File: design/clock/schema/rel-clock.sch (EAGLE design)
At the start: 15 parts, among them Q1 BC556, Q2 BS170

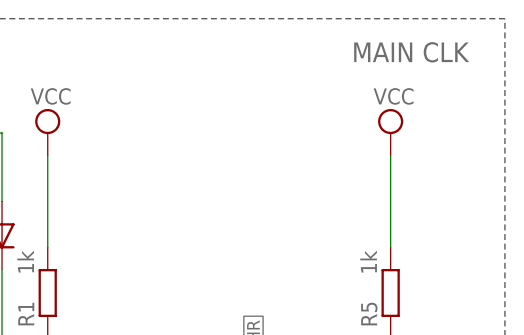
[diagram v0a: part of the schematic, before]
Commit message: Aligned titles size for all schemas
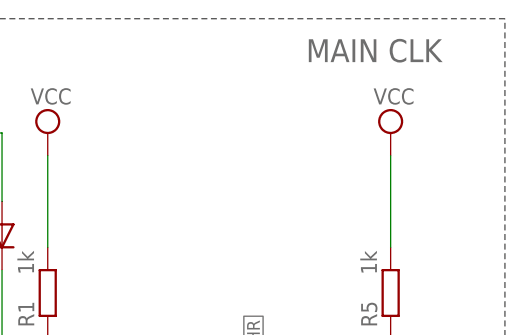
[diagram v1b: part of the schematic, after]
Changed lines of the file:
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@@
 <wire x1="203.2" y1="68.58" x2="203.2" y2="142.24" width="0.1524" layer="97" style="shortdash"/>
 <wire x1="203.2" y1="142.24" x2="66.04" y2="142.24" width="0.1524" layer="97" style="shortdash"/>
-<text x="186.182" y="137.414" size="2.1844" layer="95">MAIN CLK</text>
+<text x="181.102" y="137.414" size="2.54" layer="95">MAIN CLK</text>
 </plain>
 <instances>
